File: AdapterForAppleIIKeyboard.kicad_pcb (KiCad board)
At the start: 2 copper layers, 55.9 x 45.7 mm, 3 parts

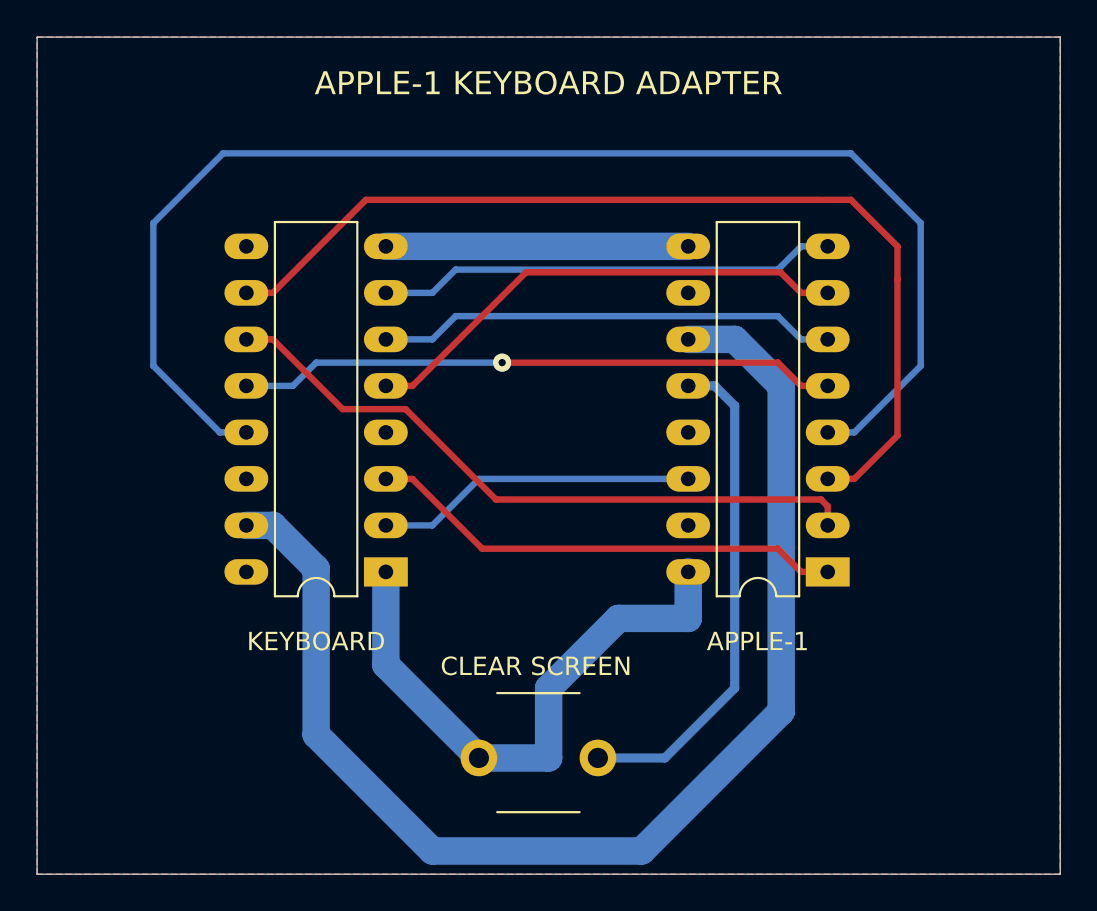
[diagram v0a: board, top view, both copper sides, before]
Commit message: added mounting holes
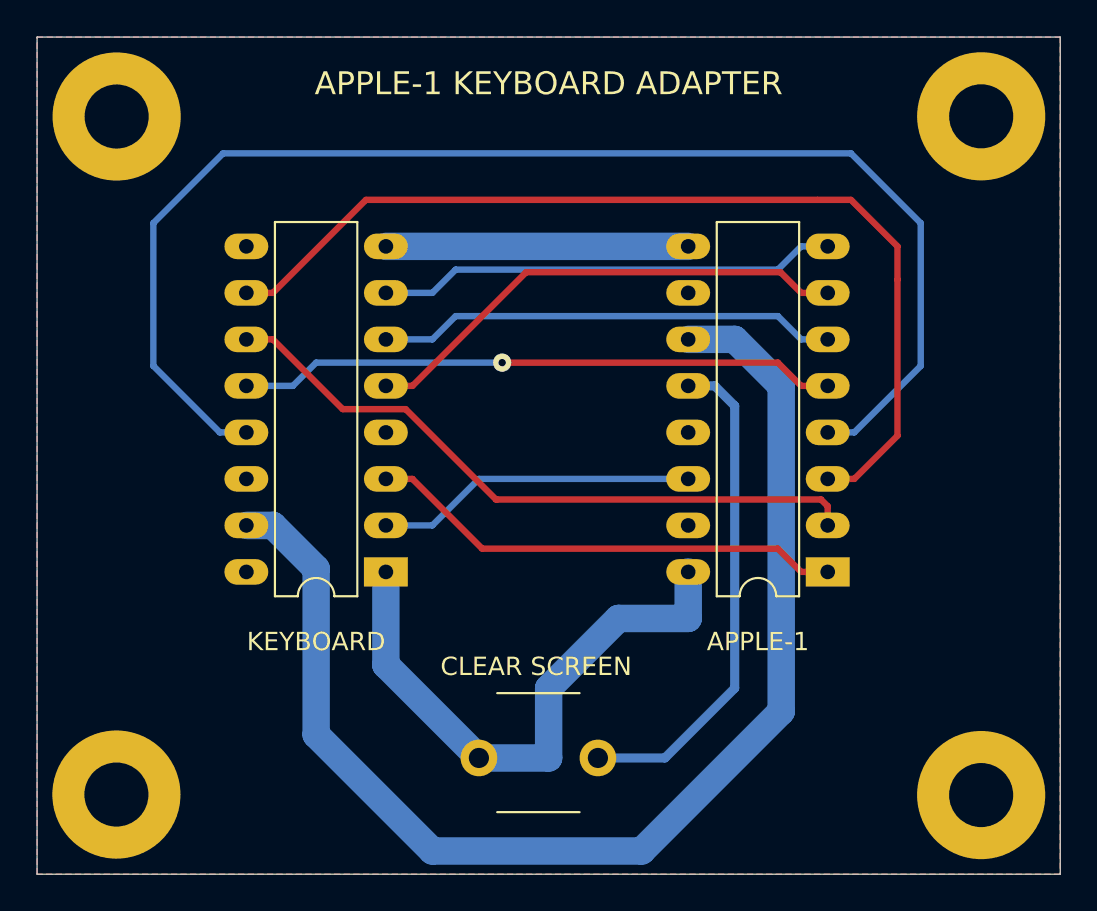
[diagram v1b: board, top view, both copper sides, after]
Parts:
- added REF**: MountingHole_3.5mm_Pad, MountingHole:MountingHole_3.5mm_Pad, F.Cu at (173.0, 119.2)
- added REF**: MountingHole_3.5mm_Pad, MountingHole:MountingHole_3.5mm_Pad, F.Cu at (173.0, 82.2)
- added REF**: MountingHole_3.5mm_Pad, MountingHole:MountingHole_3.5mm_Pad, F.Cu at (125.8, 82.2)
- added REF**: MountingHole_3.5mm_Pad, MountingHole:MountingHole_3.5mm_Pad, F.Cu at (125.8, 119.2)
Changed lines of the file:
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@@
     (tracks 79)
     (zones 0)
-    (modules 3)
+    (modules 7)
     (nets 21)
   )
@@
     (mod_text_size 1 1)
     (mod_text_width 0.15)
-    (pad_size 2.4 1.4)
-    (pad_drill 0.8)
+    (pad_size 7 7)
+    (pad_drill 3.5)
     (pad_to_mask_clearance 0.051)
     (solder_mask_min_width 0.25)
@@
     (add_net STB)
   )
+  (module MountingHole:MountingHole_3.5mm_Pad (layer F.Cu)
+    (at 172.98162 119.2276)
+    (descr "Mounting Hole 3.5mm")
+    (tags "mounting hole 3.5mm")
+    (attr virtual)
+    (fp_text reference REF** (at 0 -4.5) (layer F.SilkS) hide
+      (effects (font (size 1 1) (thickness 0.15)))
+    )
+    (fp_text value MountingHole_3.5mm_Pad (at 0 4.5) (layer F.Fab) hide
+      (effects (font (size 1 1) (thickness 0.15)))
+    )
+    (fp_circle (center 0 0) (end 3.75 0) (layer F.CrtYd) (width 0.05))
+    (fp_circle (center 0 0) (end 3.5 0) (layer Cmts.User) (width 0.15))
+    (fp_text user %R (at 0.3 0) (layer F.Fab)
+      (effects (font (size 1 1) (thickness 0.15)))
+    )
+    (pad 1 thru_hole circle (at 0 0) (size 7 7) (drill 3.5) (layers *.Cu *.Mask))
+  )
+  (module MountingHole:MountingHole_3.5mm_Pad (layer F.Cu)
+    (at 172.98416 82.15884)
+    (descr "Mounting Hole 3.5mm")
+    (tags "mounting hole 3.5mm")
+    (attr virtual)
+    (fp_text reference REF** (at 0 -4.5) (layer F.SilkS) hide
+      (effects (font (size 1 1) (thickness 0.15)))
+    )
+    (fp_text value MountingHole_3.5mm_Pad (at 0 4.5) (layer F.Fab) hide
+      (effects (font (size 1 1) (thickness 0.15)))
+    )
+    (fp_circle (center 0 0) (end 3.75 0) (layer F.CrtYd) (width 0.05))
+    (fp_circle (center 0 0) (end 3.5 0) (layer Cmts.User) (width 0.15))
+    (fp_text user %R (at 0.3 0) (layer F.Fab)
+      (effects (font (size 1 1) (thickness 0.15)))
+    )
+    (pad 1 thru_hole circle (at 0 0) (size 7 7) (drill 3.5) (layers *.Cu *.Mask))
+  )
+  (module MountingHole:MountingHole_3.5mm_Pad (layer F.Cu)
+    (at 125.7681 82.169)
+    (descr "Mounting Hole 3.5mm")
+    (tags "mounting hole 3.5mm")
+    (attr virtual)
+    (fp_text reference REF** (at 0 -4.5) (layer F.SilkS) hide
+      (effects (font (size 1 1) (thickness 0.15)))
+    )
+    (fp_text value MountingHole_3.5mm_Pad (at 0 4.5) (layer F.Fab) hide
+      (effects (font (size 1 1) (thickness 0.15)))
+    )
+    (fp_circle (center 0 0) (end 3.75 0) (layer F.CrtYd) (width 0.05))
+    (fp_circle (center 0 0) (end 3.5 0) (layer Cmts.User) (width 0.15))
+    (fp_text user %R (at 0.3 0) (layer F.Fab)
+      (effects (font (size 1 1) (thickness 0.15)))
+    )
+    (pad 1 thru_hole circle (at 0 0) (size 7 7) (drill 3.5) (layers *.Cu *.Mask))
+  )
+  (module MountingHole:MountingHole_3.5mm_Pad (layer F.Cu)
+    (at 125.7554 119.19966)
+    (descr "Mounting Hole 3.5mm")
+    (tags "mounting hole 3.5mm")
+    (attr virtual)
+    (fp_text reference REF** (at 0 -4.5) (layer F.SilkS) hide
+      (effects (font (size 1 1) (thickness 0.15)))
+    )
+    (fp_text value MountingHole_3.5mm_Pad (at 0 4.5) (layer F.Fab) hide
+      (effects (font (size 1 1) (thickness 0.15)))
+    )
+    (fp_circle (center 0 0) (end 3.75 0) (layer F.CrtYd) (width 0.05))
+    (fp_circle (center 0 0) (end 3.5 0) (layer Cmts.User) (width 0.15))
+    (fp_text user %R (at 0.3 0) (layer F.Fab)
+      (effects (font (size 1 1) (thickness 0.15)))
+    )
+    (pad 1 thru_hole circle (at 0 0) (size 7 7) (drill 3.5) (layers *.Cu *.Mask))
+  )
   (module AdapterForAppleIIKeyboard:DIP-16_W7.62mm_LongPads (layer F.Cu)
     (at 140.47216 107.04068 180)
@@
     )
     (fp_text value "CLEAR SCREEN" (at 3.1242 -2.45364) (layer F.SilkS)
-      (effects (font (size 1 1) (thickness 0.15)))
+      (effects (font (size 1 1) (thickness 0.25)))
     )
     (fp_text user %R (at 3.25 2.25) (layer F.Fab) hide
